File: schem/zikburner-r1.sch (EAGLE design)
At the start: 12 parts, among them U1 ATMEGA644-20PU, U2 FT232RLSSOP, X2 USB-SMD-NS

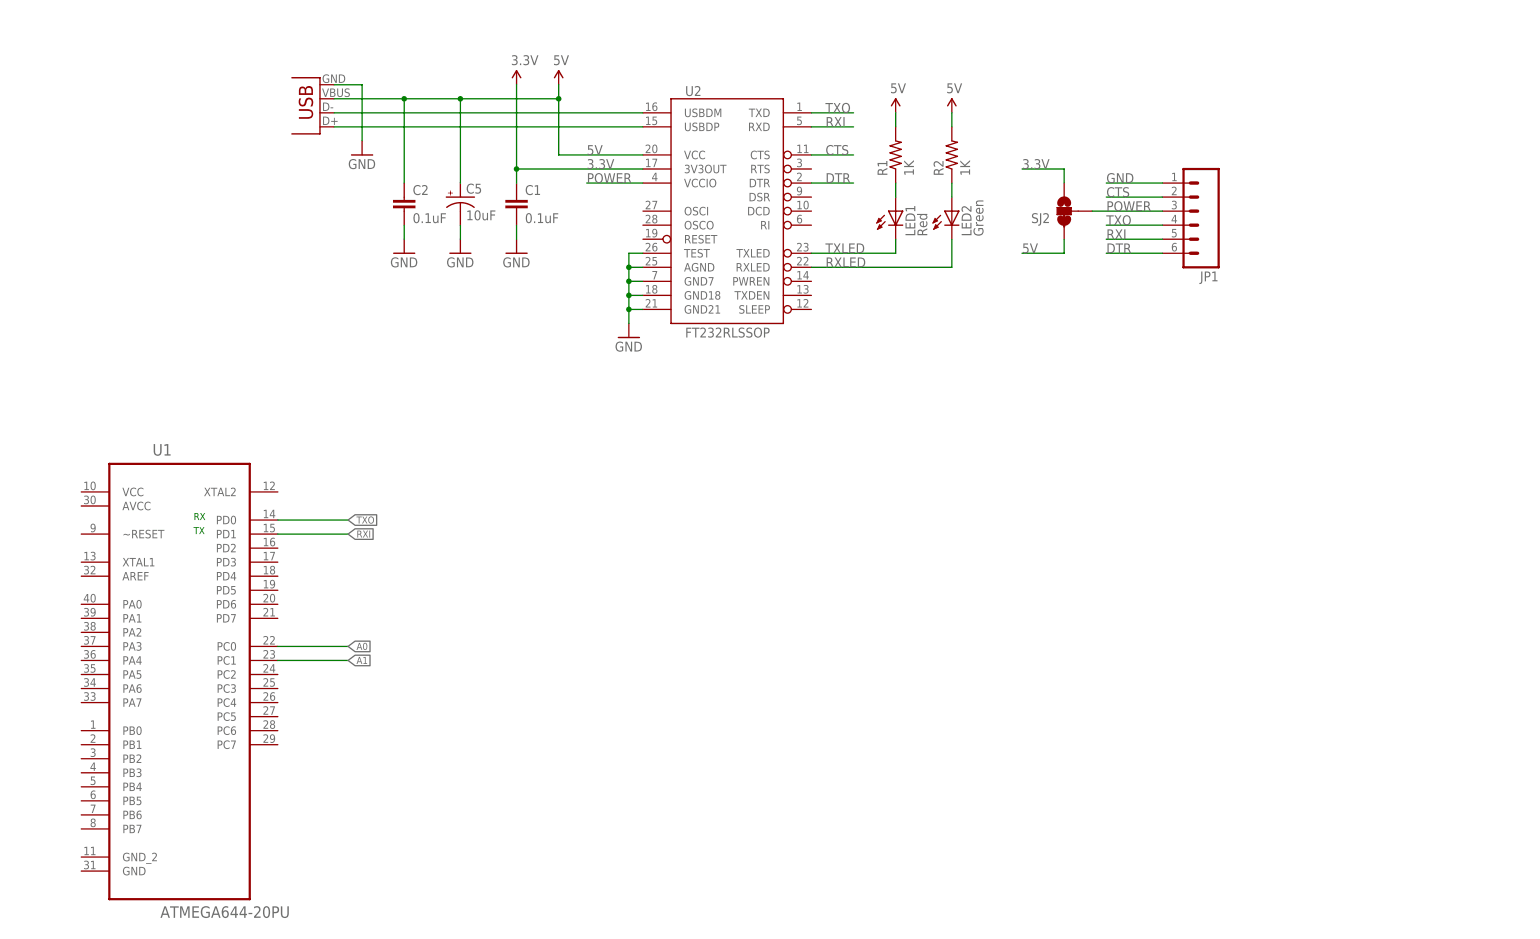
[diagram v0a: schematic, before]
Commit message: Added Eagle schematic and image
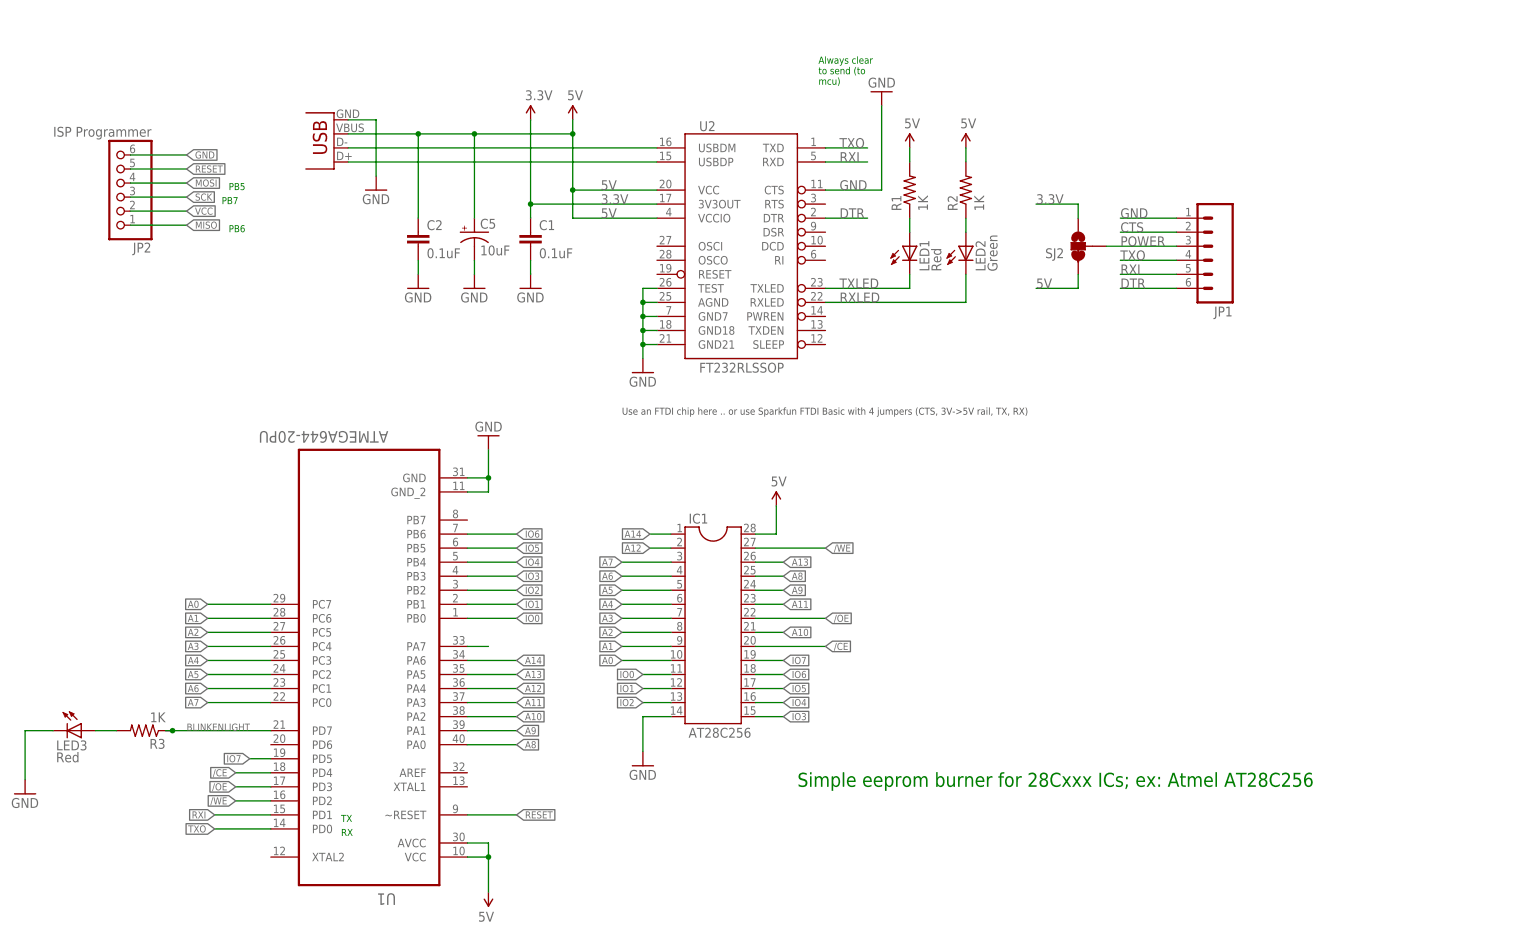
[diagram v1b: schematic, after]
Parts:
- added IC1: AT28C256, ic-package:DIL28
- added JP2: ISP Programmer, pinhead:PINHD-1X6
- added LED3: Red, SparkFun:LED0603
- added R3: 1K, SparkFun:RESISTOR0402-RES
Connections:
- new net /CE: IC1.20, U1.PD4
- new net /OE: IC1.22, U1.PD3
- new net /WE: IC1.27, U1.PD2
- new net A10: IC1.21, U1.PA2
- new net A11: IC1.23, U1.PA3
- new net A12: IC1.2, U1.PA4
- new net A13: IC1.26, U1.PA5
- new net A14: IC1.1, U1.PA6
- new net A2: IC1.8, U1.PC5
- new net A3: IC1.7, U1.PC4
- new net A4: IC1.6, U1.PC3
- new net A5: IC1.5, U1.PC2
- new net A6: IC1.4, U1.PC1
- new net A7: IC1.3, U1.PC0
- new net A8: IC1.25, U1.PA0
- new net A9: IC1.24, U1.PA1
- new net BLINKENLIGHT: R3.1, U1.PD7
- new net IO0: IC1.11, U1.PB0
- new net IO1: IC1.12, U1.PB1
- new net IO2: IC1.13, U1.PB2
- new net IO3: IC1.15, U1.PB3
- new net IO4: IC1.16, U1.PB4
- new net IO5: IC1.17, U1.PB5
- new net IO6: IC1.18, U1.PB6
- new net IO7: IC1.19, U1.PD5
- new net MISO: JP2.1
- new net MOSI: JP2.4
- new net N$4: LED3.A, R3.2
- new net N$9: U1.PA7
- new net RESET: JP2.5, U1.~RESET
- new net SCK: JP2.3
- new net VCC: JP2.2
- net 5V: now also IC1.28, U1.AVCC, U1.VCC, U2.VCCIO
- net A0: now also IC1.10, U1.PC7; no longer U1.PC0
- net A1: now also IC1.9, U1.PC6; no longer U1.PC1
- net CTS: no longer U2.CTS
- net GND: now also IC1.14, JP2.6, LED3.C, U1.GND, U1.GND_2, U2.CTS
- net POWER: no longer U2.VCCIO
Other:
- note added: "Always clear to send (to mcu)"
- note added: "PB5"
- note added: "PB6"
- note added: "PB7"
- note added: "Simple eeprom burner for 28Cxxx ICs; ex: Atmel AT28C256"
- note added: "Use an FTDI chip here .. or use Sparkfun FTDI Basic with 4 jumpers (CTS, 3V->5V rail, TX, RX)"
- moved on the sheet: C1, C2, C5, JP1, LED1, LED2, R1, R2, SJ2, U1, U2

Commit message: Fix to schematic
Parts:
- removed JP1: (no value), SparkFun:M06SMD-FEMALE-V2
- removed SJ2: (no value), SparkFun:SOLDERJUMPER_2WAYS
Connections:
- removed net CTS: JP1.2
- removed net POWER: JP1.3, SJ2.2
- net 3.3V: no longer SJ2.3
- net 5V: no longer SJ2.1
- net DTR: no longer JP1.6
- net GND: no longer JP1.1
- net RXI: no longer JP1.5
- net TXO: no longer JP1.4
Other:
- note added: "Licensed under BSD 2 clause; open source code and design. See included license file in the github."
- note added: "Simple eeprom burner for 28Cxxx ICs; ex: Atmel AT28C256 Copyright 2013 Jeff Mitchell"
- note removed: "Simple eeprom burner for 28Cxxx ICs; ex: Atmel AT28C256"
- moved on the sheet: C1, C2, C5, LED1, LED2, R1, R2, U2

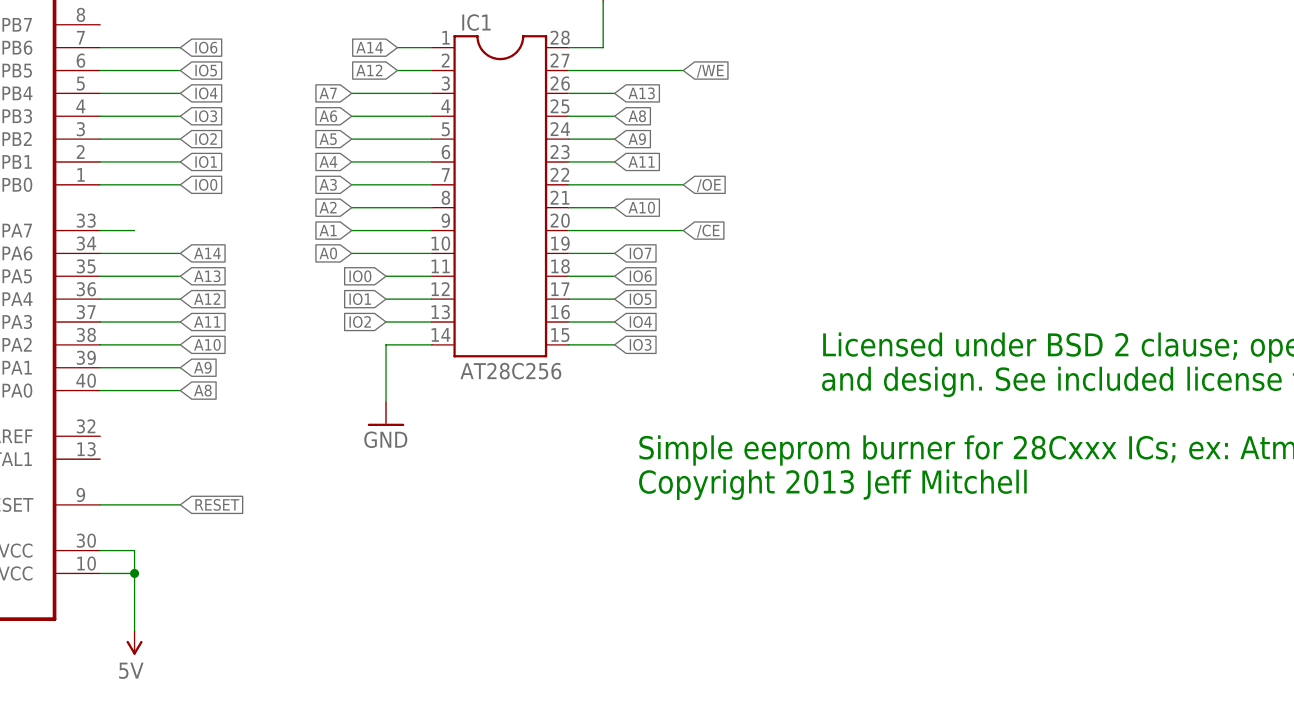
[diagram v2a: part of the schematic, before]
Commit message: Added some notes/corrections to schem (pull up on /CE, note about caps across V/GND on mcu)
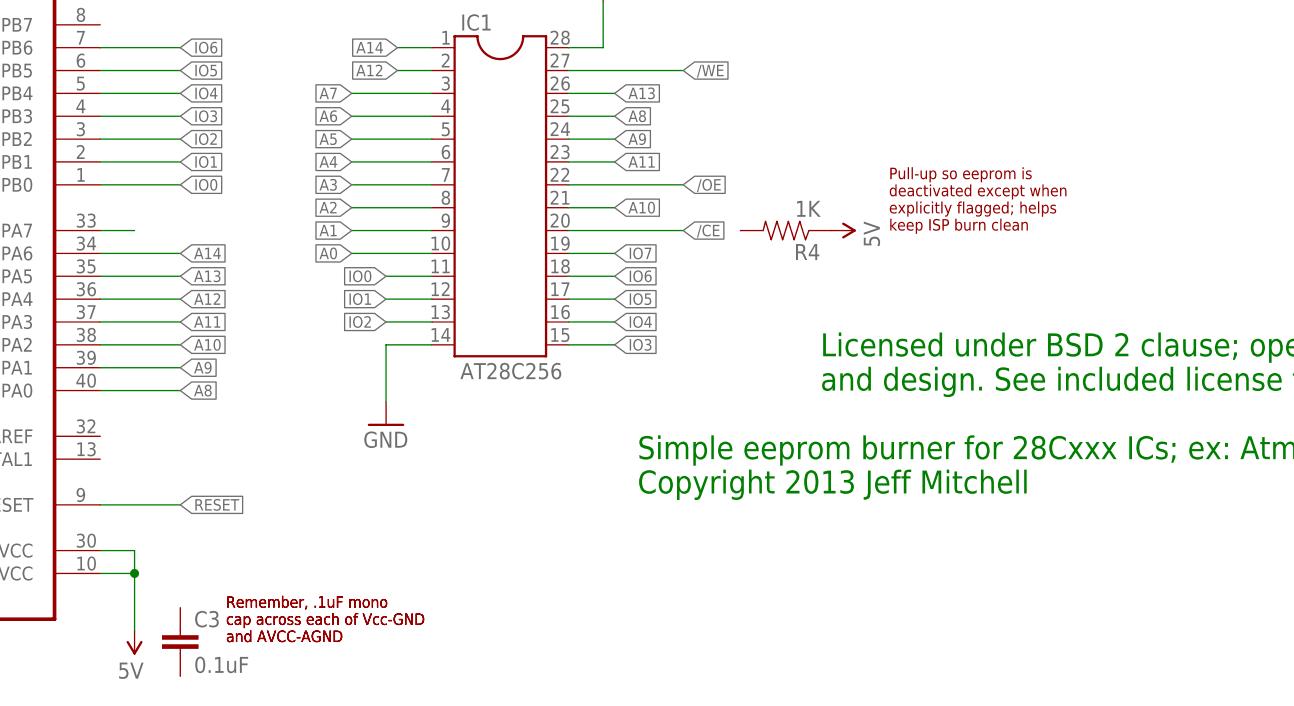
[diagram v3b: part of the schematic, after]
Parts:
- added C3: 0.1uF, SparkFun:CAP0402-CAP
- added R4: 1K, SparkFun:RESISTOR0402-RES
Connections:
- net 5V: now also R4.1
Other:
- note added: "Pull-up so eeprom is deactivated except when explicitly flagged; helps keep ISP burn clean"
- note added: "Remember, .1uF mono cap across each of Vcc-GND and AVCC-AGND"
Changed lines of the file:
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@@
 <setting verticaltext="up"/>
 </settings>
-<grid distance="0.05" unitdist="inch" unit="inch" style="dots" multiple="1" display="yes" altdistance="0.01" altunitdist="inch" altunit="inch"/>
+<grid distance="0.1" unitdist="inch" unit="inch" style="lines" multiple="1" display="no" altdistance="0.01" altunitdist="inch" altunit="inch"/>
 <layers>
 <layer number="1" name="Top" color="4" fill="1" visible="no" active="no"/>
@@
 <part name="GND9" library="SparkFun" deviceset="GND" device=""/>
 <part name="FRAME1" library="frames" deviceset="LETTER_L" device=""/>
+<part name="C3" library="SparkFun" deviceset="CAP" device="0402-CAP" value="0.1uF"/>
+<part name="R4" library="SparkFun" deviceset="RESISTOR" device="0402-RES" value="1K"/>
+<part name="U$6" library="SparkFun" deviceset="5V" device=""/>
 </parts>
 <sheets>
@@
 <text x="170.18" y="38.1" size="2.54" layer="91">Licensed under BSD 2 clause; open source code
 and design. See included license file in the github.</text>
+<text x="104.14" y="10.16" size="1.27" layer="94">Remember, .1uF mono
+cap across each of Vcc-GND
+and AVCC-AGND</text>
+<text x="104.14" y="10.16" size="1.27" layer="94">Remember, .1uF mono
+cap across each of Vcc-GND
+and AVCC-AGND</text>
+<text x="177.8" y="55.88" size="1.27" layer="94">Pull-up so eeprom is
+deactivated except when
+explicitly flagged; helps
+keep ISP burn clean</text>
 </plain>
 <instances>
@@
 <instance part="FRAME1" gate="G$1" x="0" y="0"/>
 <instance part="FRAME1" gate="G$2" x="147.32" y="0"/>
+<instance part="C3" gate="G$1" x="99.06" y="8.89"/>
+<instance part="R4" gate="G$1" x="166.37" y="55.88" rot="R180"/>
+<instance part="U$6" gate="G$1" x="171.45" y="55.88" rot="R270"/>
 </instances>
 <busses>
@@
 <junction x="93.98" y="17.78"/>
 </segment>
-</net>
+<segment>
+<pinref part="R4" gate="G$1" pin="1"/>
+<pinref part="U$6" gate="G$1" pin="5V"/>
+</segment>
+</net>
